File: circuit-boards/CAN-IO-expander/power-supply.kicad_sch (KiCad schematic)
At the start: 26 parts, among them U7 TPS613222ADBVR, U9 LMR54410FDBVR

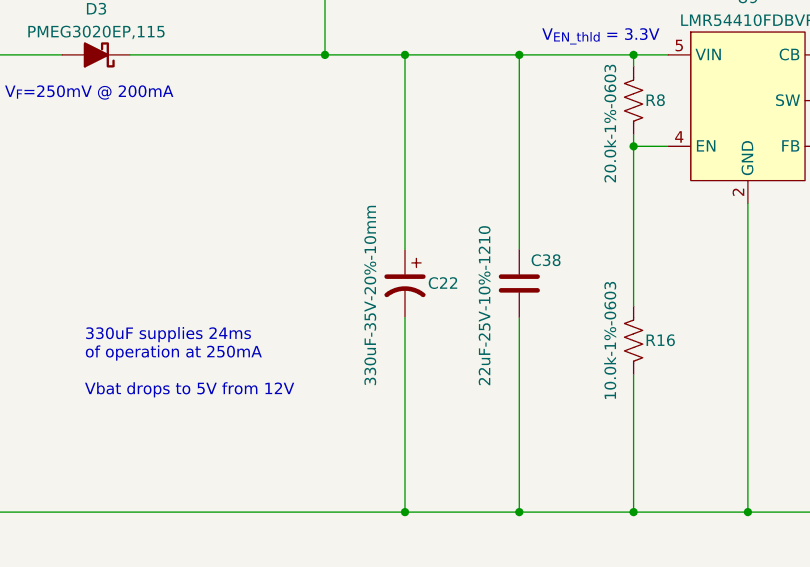
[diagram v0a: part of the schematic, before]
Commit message: Changed to 1 encoder, all connectors to SMD right angle SL
Signed-off-by: Scott Berman <sgberman1@gmail.com>
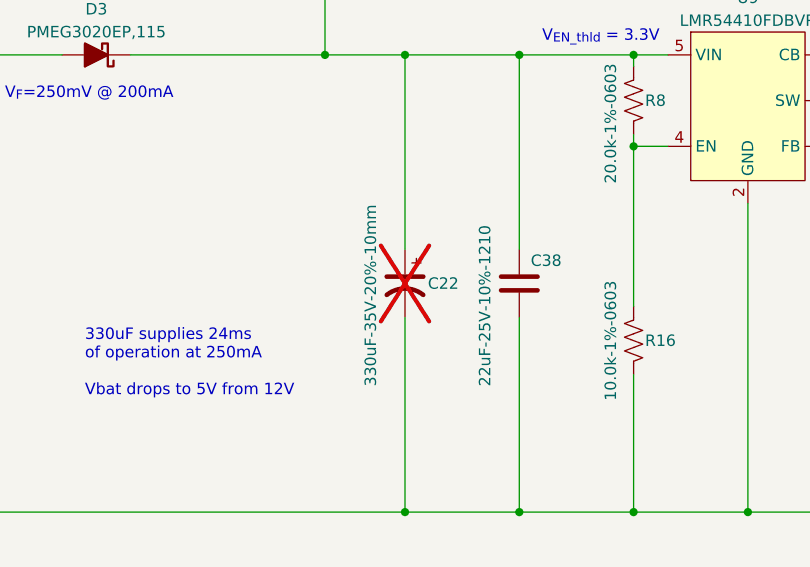
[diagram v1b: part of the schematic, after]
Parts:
- C22: now not fitted; now left out of the parts list
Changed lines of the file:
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@@
 		(unit 1)
 		(exclude_from_sim no)
-		(in_bom yes)
-		(on_board yes)
-		(dnp no)
+		(in_bom no)
+		(on_board no)
+		(dnp yes)
 		(property "Reference" "C22"
 			(at 204.47 104.14 0)
